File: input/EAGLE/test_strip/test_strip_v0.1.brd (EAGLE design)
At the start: 121.9 x 168.9 mm, 8 parts, among them X1 BU-SMA-E-ND, X2 BU-SMA-E-ND, X3 BU-SMA-E-ND, X4 BU-SMA-E-ND, X5 BU-SMA-E-ND, X6 BU-SMA-E-ND, X7 BU-SMA-E-ND, X8 BU-SMA-E-ND

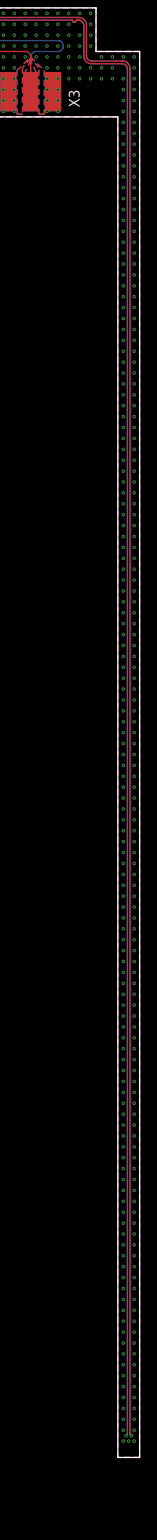
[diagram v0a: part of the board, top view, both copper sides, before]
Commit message: - Added fixed strip
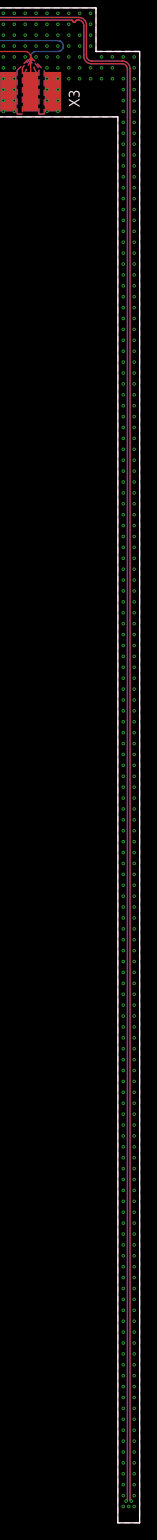
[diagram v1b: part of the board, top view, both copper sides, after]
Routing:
- net SIGA_P: track 563.0 -> 578.2 mm
- net SIGA_N: track 564.0 -> 579.2 mm
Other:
- board size 121.9 x 168.9 mm -> 121.9 x 176.5 mm
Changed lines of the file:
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@@
 <setting verticaltext="up"/>
 </settings>
-<grid distance="25" unitdist="mil" unit="mil" style="lines" multiple="1" display="yes" altdistance="12.5" altunitdist="mil" altunit="mil"/>
+<grid distance="0.05" unitdist="inch" unit="inch" style="lines" multiple="1" display="yes" altdistance="0.025" altunitdist="inch" altunit="inch"/>
 <layers>
 <layer number="1" name="Top" color="16" fill="1" visible="yes" active="yes"/>
@@
 <wire x1="-28.575" y1="6.35" x2="-28.575" y2="-3.81" width="0.000003125" layer="20"/>
 <wire x1="-28.575" y1="-3.81" x2="31.115" y2="-3.81" width="0.000003125" layer="20"/>
-<wire x1="31.115" y1="-3.81" x2="31.115" y2="-160.02" width="0.000003125" layer="20"/>
-<wire x1="31.115" y1="-160.02" x2="33.655" y2="-160.02" width="0.000003125" layer="20"/>
-<wire x1="33.655" y1="-160.02" x2="33.655" y2="3.81" width="0.000003125" layer="20"/>
+<wire x1="31.115" y1="-3.81" x2="31.115" y2="-167.64" width="0.000003125" layer="20"/>
+<wire x1="31.115" y1="-167.64" x2="33.655" y2="-167.64" width="0.000003125" layer="20"/>
+<wire x1="33.655" y1="-167.64" x2="33.655" y2="3.81" width="0.000003125" layer="20"/>
 <wire x1="33.655" y1="3.81" x2="28.575" y2="3.81" width="0.000003125" layer="20"/>
 <wire x1="28.575" y1="3.81" x2="28.575" y2="8.89" width="0.000003125" layer="20"/>
@@
 <vertex x="28.575" y="3.81"/>
 <vertex x="33.655" y="3.81"/>
-<vertex x="33.655" y="-160.02"/>
-<vertex x="31.115" y="-160.02"/>
+<vertex x="33.655" y="-167.64"/>
+<vertex x="31.115" y="-167.64"/>
 <vertex x="31.115" y="-3.81"/>
 <vertex x="-28.575" y="-3.81"/>
@@
 <via x="31.75" y="-37.465" extent="1-16" drill="0.2032"/>
 <via x="31.75" y="-38.735" extent="1-16" drill="0.2032"/>
-<via x="31.75" y="-156.845" extent="1-16" drill="0.2032"/>
-<via x="33.02" y="-156.845" extent="1-16" drill="0.2032"/>
+<via x="31.75" y="-164.465" extent="1-16" drill="0.2032"/>
+<via x="33.02" y="-164.465" extent="1-16" drill="0.2032"/>
 <via x="33.02" y="-155.575" extent="1-16" drill="0.2032"/>
 <via x="33.02" y="-154.305" extent="1-16" drill="0.2032"/>
@@
 <via x="31.75" y="-98.425" extent="1-16" drill="0.2032"/>
 <via x="31.75" y="-99.695" extent="1-16" drill="0.2032"/>
-<via x="31.75" y="-158.115" extent="1-16" drill="0.2032"/>
-<via x="33.02" y="-158.115" extent="1-16" drill="0.2032"/>
-<via x="32.385" y="-158.115" extent="1-16" drill="0.2032"/>
+<via x="31.75" y="-165.735" extent="1-16" drill="0.2032"/>
+<via x="33.02" y="-165.735" extent="1-16" drill="0.2032"/>
+<via x="32.385" y="-165.735" extent="1-16" drill="0.2032"/>
 <via x="17.78" y="6.985" extent="1-16" drill="0.2032"/>
 <via x="17.78" y="8.255" extent="1-16" drill="0.2032"/>
@@
 <vertex x="28.575" y="3.81"/>
 <vertex x="33.655" y="3.81"/>
-<vertex x="33.655" y="-160.02"/>
-<vertex x="31.115" y="-160.02"/>
+<vertex x="33.655" y="-167.64"/>
+<vertex x="31.115" y="-167.64"/>
 <vertex x="31.115" y="-3.81"/>
 <vertex x="-28.575" y="-3.81"/>
@@
 <vertex x="28.575" y="3.81"/>
 <vertex x="33.655" y="3.81"/>
-<vertex x="33.655" y="-160.02"/>
-<vertex x="31.115" y="-160.02"/>
+<vertex x="33.655" y="-167.64"/>
+<vertex x="31.115" y="-167.64"/>
 <vertex x="31.115" y="-3.81"/>
 <vertex x="-28.575" y="-3.81"/>
@@
 <vertex x="28.575" y="3.81"/>
 <vertex x="33.655" y="3.81"/>
-<vertex x="33.655" y="-160.02"/>
-<vertex x="31.115" y="-160.02"/>
+<vertex x="33.655" y="-167.64"/>
+<vertex x="31.115" y="-167.64"/>
 <vertex x="31.115" y="-3.81"/>
 <vertex x="-28.575" y="-3.81"/>
@@
 <via x="29.21" y="0.635" extent="1-16" drill="0.2032"/>
 <via x="30.48" y="0.635" extent="1-16" drill="0.2032"/>
+<via x="33.02" y="-160.655" extent="1-16" drill="0.2032"/>
+<via x="33.02" y="-159.385" extent="1-16" drill="0.2032"/>
+<via x="31.75" y="-159.385" extent="1-16" drill="0.2032"/>
+<via x="31.75" y="-160.655" extent="1-16" drill="0.2032"/>
+<via x="31.75" y="-158.115" extent="1-16" drill="0.2032"/>
+<via x="33.02" y="-158.115" extent="1-16" drill="0.2032"/>
+<via x="33.02" y="-156.845" extent="1-16" drill="0.2032"/>
+<via x="31.75" y="-156.845" extent="1-16" drill="0.2032"/>
+<via x="31.75" y="-161.925" extent="1-16" drill="0.2032"/>
+<via x="33.02" y="-161.925" extent="1-16" drill="0.2032"/>
+<via x="31.75" y="-163.195" extent="1-16" drill="0.2032"/>
+<via x="33.02" y="-163.195" extent="1-16" drill="0.2032"/>
 </signal>
 <signal name="SIGA_P">
@@
 <wire x1="28.0416" y1="2.3876" x2="31.5976" y2="2.3876" width="0.1524" layer="16"/>
 <wire x1="31.5976" y1="2.3876" x2="32.2326" y2="1.7526" width="0.1524" layer="16" curve="-90"/>
-<wire x1="32.2326" y1="1.7526" x2="32.2326" y2="-157.3276" width="0.1524" layer="16"/>
-<wire x1="32.2326" y1="-157.3276" x2="32.0802" y2="-157.48" width="0.1524" layer="16" curve="-90"/>
-<via x="32.0802" y="-157.48" extent="1-16" drill="0.2032"/>
-<wire x1="32.2326" y1="-157.3276" x2="32.2326" y2="1.7526" width="0.1524" layer="1"/>
+<wire x1="32.2326" y1="1.7526" x2="32.2326" y2="-164.9476" width="0.1524" layer="16"/>
+<wire x1="32.2326" y1="-164.9476" x2="32.0802" y2="-165.1" width="0.1524" layer="16" curve="-90"/>
+<via x="32.0802" y="-165.1" extent="1-16" drill="0.2032"/>
+<wire x1="32.2326" y1="-164.9476" x2="32.2326" y2="1.7526" width="0.1524" layer="1"/>
 <wire x1="32.2326" y1="1.7526" x2="31.5976" y2="2.3876" width="0.1524" layer="1" curve="90"/>
 <wire x1="28.0416" y1="2.3876" x2="31.5976" y2="2.3876" width="0.1524" layer="1"/>
@@
 <wire x1="26.5176" y1="7.4676" x2="26.3271" y2="7.4676" width="0.1524" layer="16"/>
 <wire x1="-85.725" y1="7.3152" x2="-85.5726" y2="7.4676" width="0.1524" layer="1" curve="-90"/>
-<wire x1="32.0802" y1="-157.48" x2="32.2326" y2="-157.3276" width="0.1524" layer="1" curve="90"/>
+<wire x1="32.0802" y1="-165.1" x2="32.2326" y2="-164.9476" width="0.1524" layer="1" curve="90"/>
 <wire x1="25.75578125" y1="7.4676" x2="-85.5726" y2="7.4676" width="0.1524" layer="16"/>
 </signal>
@@
 <wire x1="28.0924" y1="2.6924" x2="31.6484" y2="2.6924" width="0.1524" layer="16"/>
 <wire x1="31.6484" y1="2.6924" x2="32.5374" y2="1.8034" width="0.1524" layer="16" curve="-90"/>
-<wire x1="32.5374" y1="1.8034" x2="32.5374" y2="-157.3276" width="0.1524" layer="16"/>
-<wire x1="32.5374" y1="-157.3276" x2="32.6898" y2="-157.48" width="0.1524" layer="16" curve="90"/>
-<via x="32.6898" y="-157.48" extent="1-16" drill="0.2032"/>
-<wire x1="32.5374" y1="-157.3276" x2="32.5374" y2="1.8034" width="0.1524" layer="1"/>
+<wire x1="32.5374" y1="1.8034" x2="32.5374" y2="-164.9476" width="0.1524" layer="16"/>
+<wire x1="32.5374" y1="-164.9476" x2="32.6898" y2="-165.1" width="0.1524" layer="16" curve="90"/>
+<via x="32.6898" y="-165.1" extent="1-16" drill="0.2032"/>
+<wire x1="32.5374" y1="-164.9476" x2="32.5374" y2="1.8034" width="0.1524" layer="1"/>
 <wire x1="32.5374" y1="1.8034" x2="31.6484" y2="2.6924" width="0.1524" layer="1" curve="90"/>
 <wire x1="28.0924" y1="2.6924" x2="31.6484" y2="2.6924" width="0.1524" layer="1"/>
@@
 </polygon>
 <wire x1="-85.725" y1="7.9248" x2="-85.5726" y2="7.7724" width="0.1524" layer="1" curve="90"/>
-<wire x1="32.6898" y1="-157.48" x2="32.5374" y2="-157.3276" width="0.1524" layer="1" curve="-90"/>
+<wire x1="32.6898" y1="-165.1" x2="32.5374" y2="-164.9476" width="0.1524" layer="1" curve="-90"/>
 </signal>
 <signal name="SIGB_P">
